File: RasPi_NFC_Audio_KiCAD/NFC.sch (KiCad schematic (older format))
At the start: 35 parts, among them U2 PN532, Y1 Oscillator

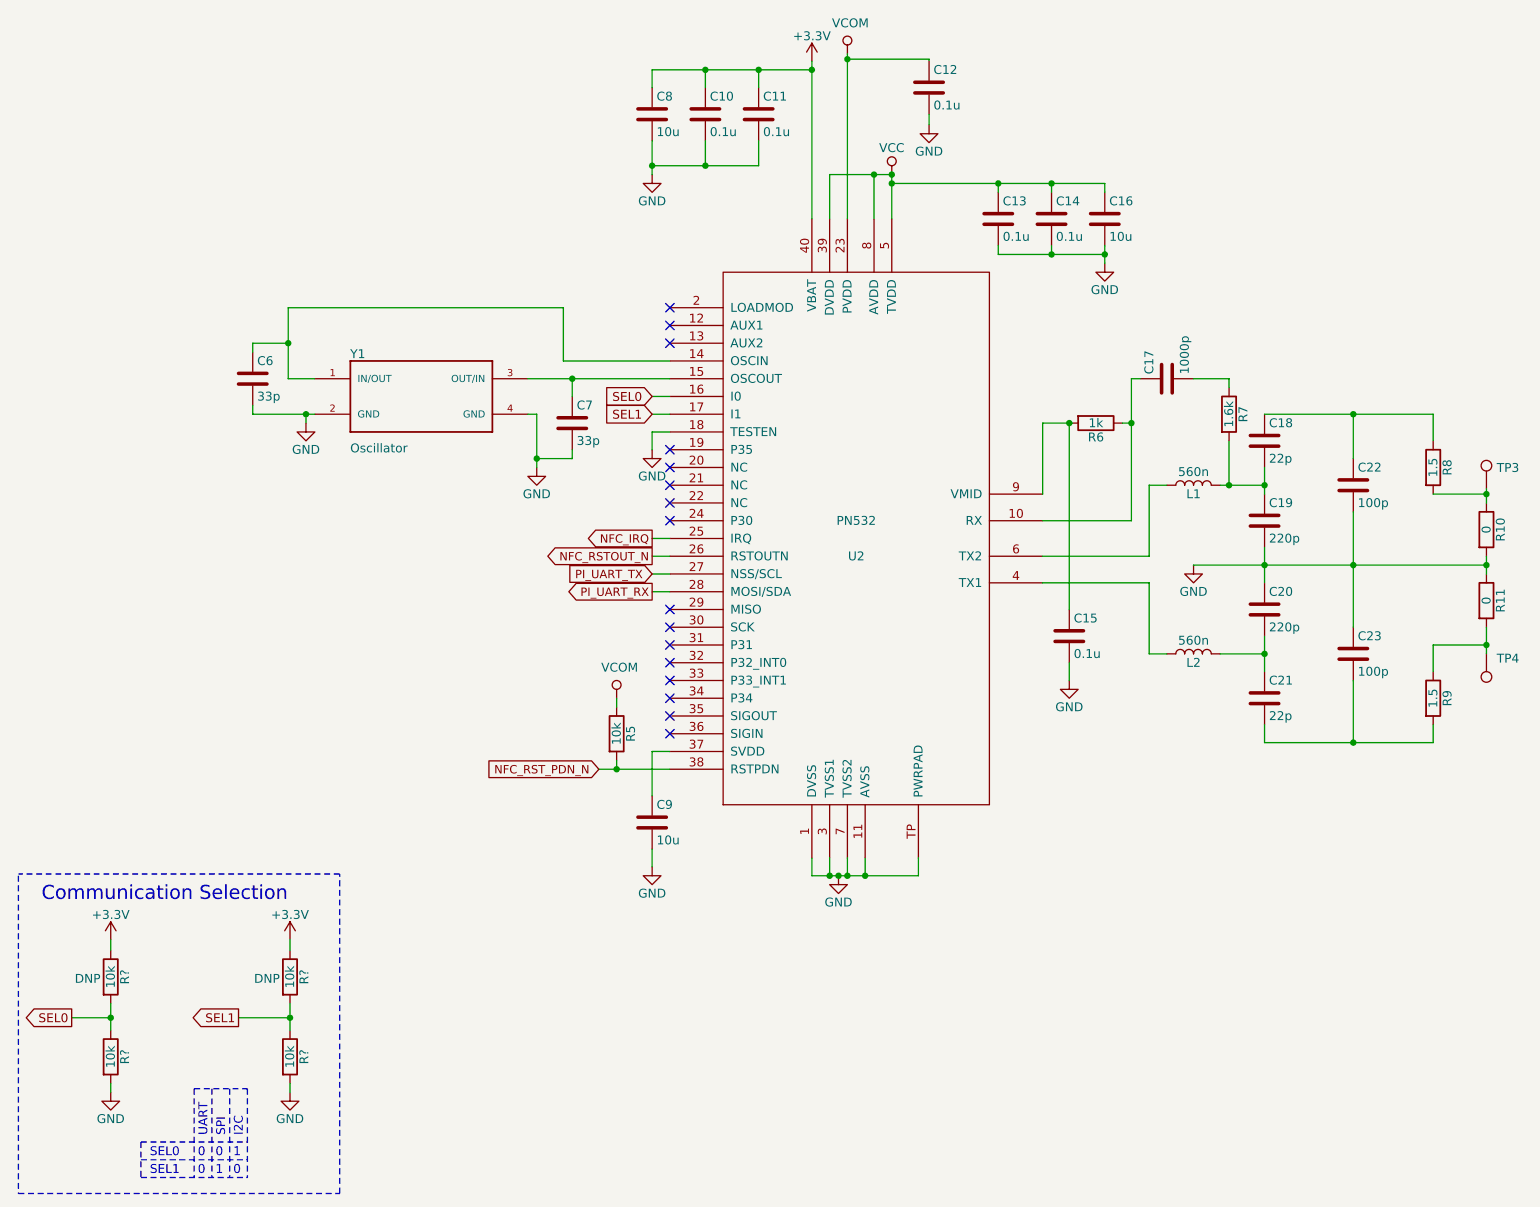
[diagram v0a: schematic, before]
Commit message: Startednfootprint assignment
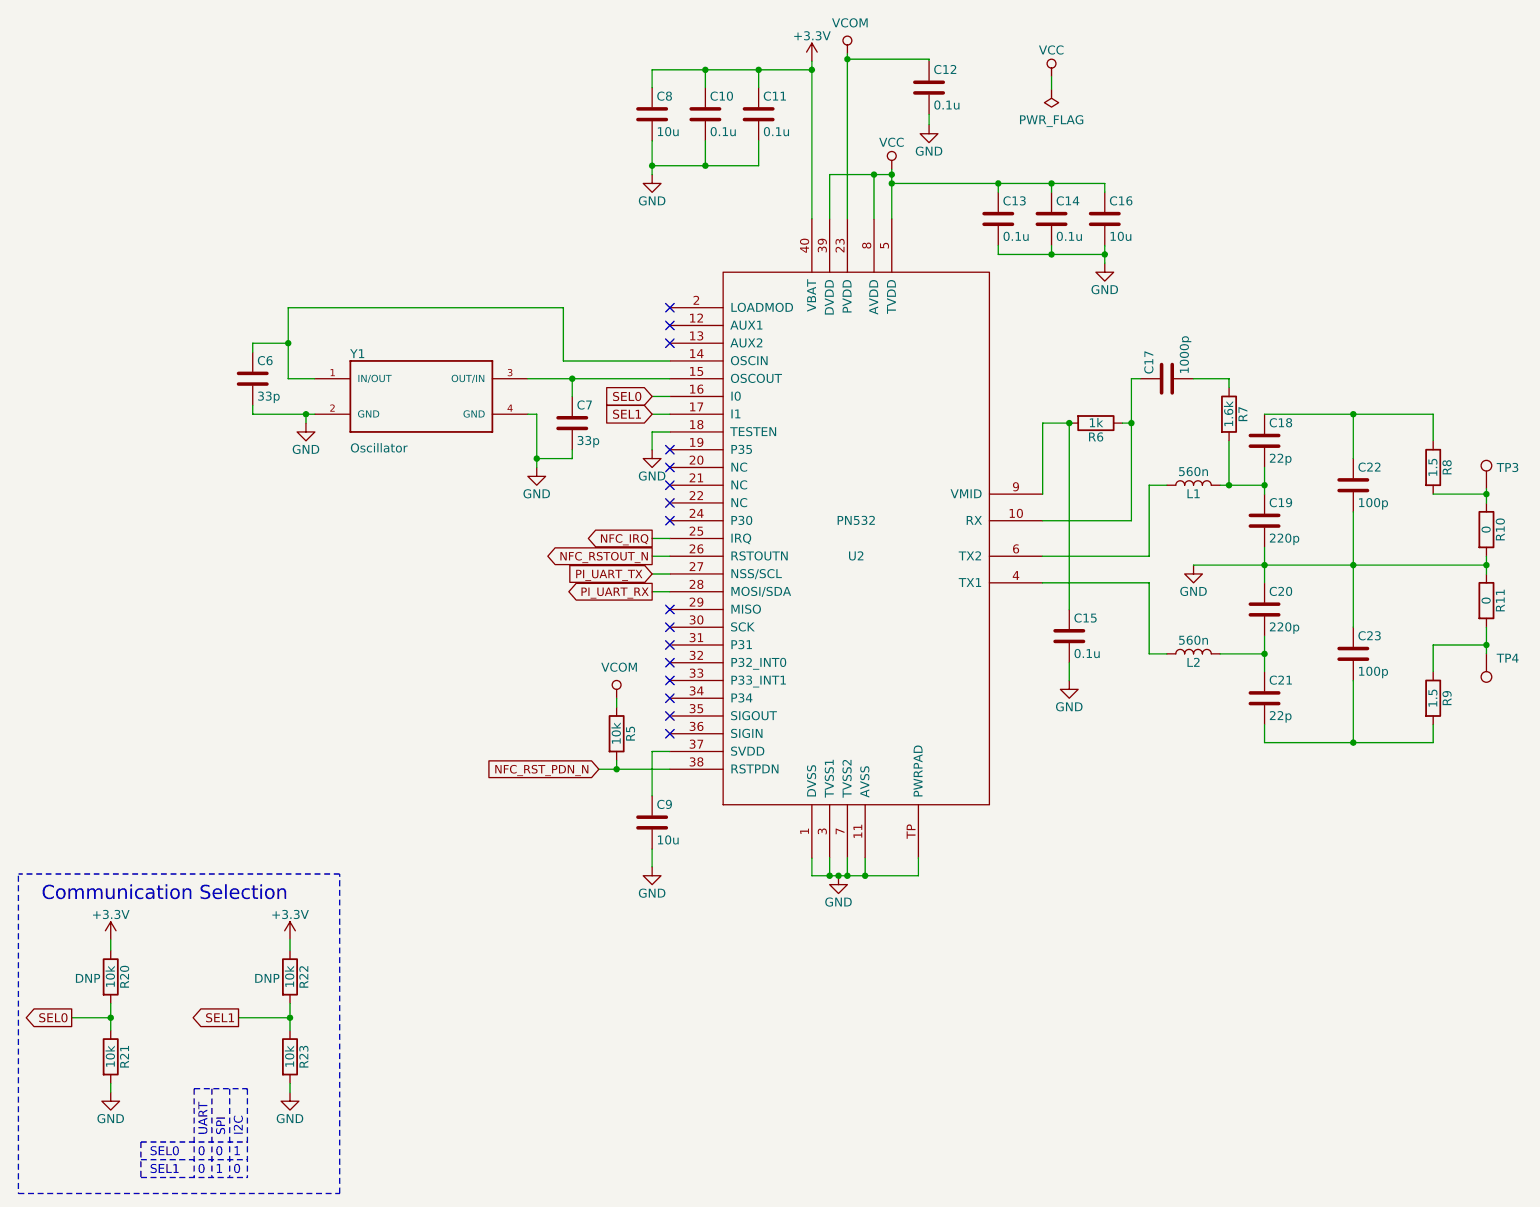
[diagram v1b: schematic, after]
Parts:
- C10, C11, C12, C13, C14, C15, C17, C18, C19, C20, C21, C22, C23, C6, C7: footprint Capacitors_SMD:C_0402 -> Capacitor_SMD:C_0603_1608Metric_Pad1.05x0.95mm_HandSolder
- C16, C8, C9: footprint Capacitors_SMD:C_0603_HandSoldering -> Capacitor_SMD:C_0603_1608Metric_Pad1.05x0.95mm_HandSolder
- R10, R11: footprint Resistors_SMD:R_0402 -> Resistor_SMD:R_0603_1608Metric_Pad1.05x0.95mm_HandSolder
- R20, R21, R22, R23: renamed from R?; footprint Resistors_SMD:R_0603_HandSoldering -> Resistor_SMD:R_0603_1608Metric_Pad1.05x0.95mm_HandSolder
- R5, R6, R7, R8, R9: footprint Resistors_SMD:R_0603_HandSoldering -> Resistor_SMD:R_0603_1608Metric_Pad1.05x0.95mm_HandSolder
- U2: footprint NFC_Toy_Lib:HVQFN40-6X6 -> RasPi_NFC_Audio_PCB_Lib:HVQFN40-6X6
- Y1: footprint NFC_Toy_Lib:OSCCC500X320X105N -> RasPi_NFC_Audio_PCB_Lib:OSCCC500X320X105N

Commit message: Layout started
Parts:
- L1, L2: footprint Inductors_SMD:L_0603_HandSoldering -> Inductor_SMD:L_0603_1608Metric_Pad1.05x0.95mm_HandSolder
- R10, R11: footprint Resistor_SMD:R_0603_1608Metric_Pad1.05x0.95mm_HandSolder -> Resistor_SMD:R_0402_1005Metric; DigiKey 311-0.0GRCT-ND -> 1276-3480-1-ND; Part # RC0603JR-070RL -> RC1005J000CS
- TP3, TP4: footprint (none) -> TestPoint:TestPoint_Pad_2.0x2.0mm
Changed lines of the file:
@@
 F 0 "L1" V 8250 3440 50  0000 C CNN
 F 1 "560n" V 8375 3440 50  0000 C CNN
-F 2 "Inductors_SMD:L_0603_HandSoldering" H 8300 3440 50  0001 C CNN
+F 2 "Inductor_SMD:L_0603_1608Metric_Pad1.05x0.95mm_HandSolder" H 8300 3440 50  0001 C CNN
 F 3 "" H 8300 3440 50  0001 C CNN
 F 4 "MLJ1608WR56JT000" H 8300 3440 50  0001 C CNN "Part #"
@@
 F 0 "L2" V 8250 4390 50  0000 C CNN
 F 1 "560n" V 8375 4390 50  0000 C CNN
-F 2 "Inductors_SMD:L_0603_HandSoldering" H 8300 4390 50  0001 C CNN
+F 2 "Inductor_SMD:L_0603_1608Metric_Pad1.05x0.95mm_HandSolder" H 8300 4390 50  0001 C CNN
 F 3 "" H 8300 4390 50  0001 C CNN
 F 4 "MLJ1608WR56JT000" H 8300 4390 50  0001 C CNN "Part #"
@@
 F 0 "R10" V 10030 3690 50  0000 C CNN
 F 1 "0" V 9950 3690 50  0000 C CNN
-F 2 "Resistor_SMD:R_0603_1608Metric_Pad1.05x0.95mm_HandSolder" V 9880 3690 50  0001 C CNN
+F 2 "Resistor_SMD:R_0402_1005Metric" V 9880 3690 50  0001 C CNN
 F 3 "" H 9950 3690 50  0001 C CNN
-F 4 "RC0603JR-070RL" H 9950 3690 50  0001 C CNN "Part #"
-F 5 "311-0.0GRCT-ND" H 9950 3690 50  0001 C CNN "DigiKey"
+F 4 "RC1005J000CS" H 9950 3690 50  0001 C CNN "Part #"
+F 5 "1276-3480-1-ND" H 9950 3690 50  0001 C CNN "DigiKey"
 	1    9950 3690
 	1    0    0    -1
@@
 F 0 "R11" V 10030 4090 50  0000 C CNN
 F 1 "0" V 9950 4090 50  0000 C CNN
-F 2 "Resistor_SMD:R_0603_1608Metric_Pad1.05x0.95mm_HandSolder" V 9880 4090 50  0001 C CNN
+F 2 "Resistor_SMD:R_0402_1005Metric" V 9880 4090 50  0001 C CNN
 F 3 "" H 9950 4090 50  0001 C CNN
-F 4 "RC0603JR-070RL" H 9950 4090 50  0001 C CNN "Part #"
-F 5 "311-0.0GRCT-ND" H 9950 4090 50  0001 C CNN "DigiKey"
+F 4 "RC1005J000CS" H 9950 4090 50  0001 C CNN "Part #"
+F 5 "1276-3480-1-ND" H 9950 4090 50  0001 C CNN "DigiKey"
 	1    9950 4090
 	1    0    0    -1
@@
 F 0 "TP3" H 10008 3578 50  0000 L CNN
 F 1 "TestPoint" H 10008 3487 50  0001 L CNN
-F 2 "" H 10150 3460 50  0001 C CNN
+F 2 "TestPoint:TestPoint_Pad_2.0x2.0mm" H 10150 3460 50  0001 C CNN
 F 3 "~" H 10150 3460 50  0001 C CNN
 	1    9950 3460
@@
 F 0 "TP4" H 9892 4416 50  0000 R CNN
 F 1 "TestPoint" H 9892 4507 50  0001 R CNN
-F 2 "" H 10150 4390 50  0001 C CNN
+F 2 "TestPoint:TestPoint_Pad_2.0x2.0mm" H 10150 4390 50  0001 C CNN
 F 3 "~" H 10150 4390 50  0001 C CNN
 	1    9950 4390

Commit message: Layout updates
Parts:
- TP3, TP4: footprint TestPoint:TestPoint_Pad_2.0x2.0mm -> TestPoint:TestPoint_Pad_1.0x1.0mm
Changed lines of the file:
@@
 EESchema Schematic File Version 4
 LIBS:RasPi_NFC_Audio_KiCAD-cache
-EELAYER 30 0
+EELAYER 29 0
 EELAYER END
 $Descr A4 11693 8268
@@
 F 0 "TP3" H 10008 3578 50  0000 L CNN
 F 1 "TestPoint" H 10008 3487 50  0001 L CNN
-F 2 "TestPoint:TestPoint_Pad_2.0x2.0mm" H 10150 3460 50  0001 C CNN
+F 2 "TestPoint:TestPoint_Pad_1.0x1.0mm" H 10150 3460 50  0001 C CNN
 F 3 "~" H 10150 3460 50  0001 C CNN
 	1    9950 3460
@@
 F 0 "TP4" H 9892 4416 50  0000 R CNN
 F 1 "TestPoint" H 9892 4507 50  0001 R CNN
-F 2 "TestPoint:TestPoint_Pad_2.0x2.0mm" H 10150 4390 50  0001 C CNN
+F 2 "TestPoint:TestPoint_Pad_1.0x1.0mm" H 10150 4390 50  0001 C CNN
 F 3 "~" H 10150 4390 50  0001 C CNN
 	1    9950 4390

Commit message: Layout updates
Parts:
- removed TP3, TP4: TestPoint, TestPoint:TestPoint_Pad_1.0x1.0mm, symbol Connector:TestPoint
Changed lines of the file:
@@
 	9650 3490 9950 3490
-Wire Wire Line
-	9950 3460 9950 3490
 Wire Wire Line
 	9650 4490 9650 4340
@@
 NoConn ~ 5350 2540
 NoConn ~ 5350 2640
-Connection ~ 9950 4340
-Connection ~ 9950 3490
 Wire Wire Line
 	6750 5640 6750 5540
@@
 	5550 1640 5850 1640
 Wire Wire Line
-	9950 4340 9950 4390
-Wire Wire Line
 	9950 3490 9950 3540
 Wire Wire Line
 	6450 5640 6750 5640
-$Comp
-L Connector:TestPoint TP3
-U 1 1 5E181FE8
-P 9950 3460
-F 0 "TP3" H 10008 3578 50  0000 L CNN
-F 1 "TestPoint" H 10008 3487 50  0001 L CNN
-F 2 "TestPoint:TestPoint_Pad_1.0x1.0mm" H 10150 3460 50  0001 C CNN
-F 3 "~" H 10150 3460 50  0001 C CNN
-	1    9950 3460
-	1    0    0    -1
-$EndComp
-$Comp
-L Connector:TestPoint TP4
-U 1 1 5E1839E2
-P 9950 4390
-F 0 "TP4" H 9892 4416 50  0000 R CNN
-F 1 "TestPoint" H 9892 4507 50  0001 R CNN
-F 2 "TestPoint:TestPoint_Pad_1.0x1.0mm" H 10150 4390 50  0001 C CNN
-F 3 "~" H 10150 4390 50  0001 C CNN
-	1    9950 4390
-	-1   0    0    1
-$EndComp
 Text GLabel 5250 2940 0    50   Input ~ 0
 SEL0
